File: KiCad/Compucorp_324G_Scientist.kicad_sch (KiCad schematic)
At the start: 0 parts

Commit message: Updates to schematic
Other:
- added sheet Processor Board (Compucorp_324G_Processor_Board.kicad_sch)
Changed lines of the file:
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@@
+	)
+	(sheet
+		(at 237.49 99.06)
+		(size 38.1 22.86)
+		(exclude_from_sim no)
+		(in_bom yes)
+		(on_board yes)
+		(dnp no)
+		(fields_autoplaced yes)
+		(stroke
+			(width 0.1524)
+			(type solid)
+		)
+		(fill
+			(color 0 0 0 0.0000)
+		)
+		(property "Sheetname" "Processor Board"
+			(at 237.49 98.3484 0)
+			(effects
+				(font
+					(size 1.27 1.27)
+				)
+				(justify left bottom)
+			)
+		)
+		(property "Sheetfile" "Compucorp_324G_Processor_Board.kicad_sch"
+			(at 237.49 122.5046 0)
+			(effects
+				(font
+					(size 1.27 1.27)
+				)
+				(justify left top)
+			)
+		)
+		(instances
+			(project "Compucorp_324G_Scientist"
+				(path "/2d77b643-896b-4ca4-ac76-7c6cc0d5263f"
+					(page "4")
+				)
+			)
+		)
 	)
 	(sheet

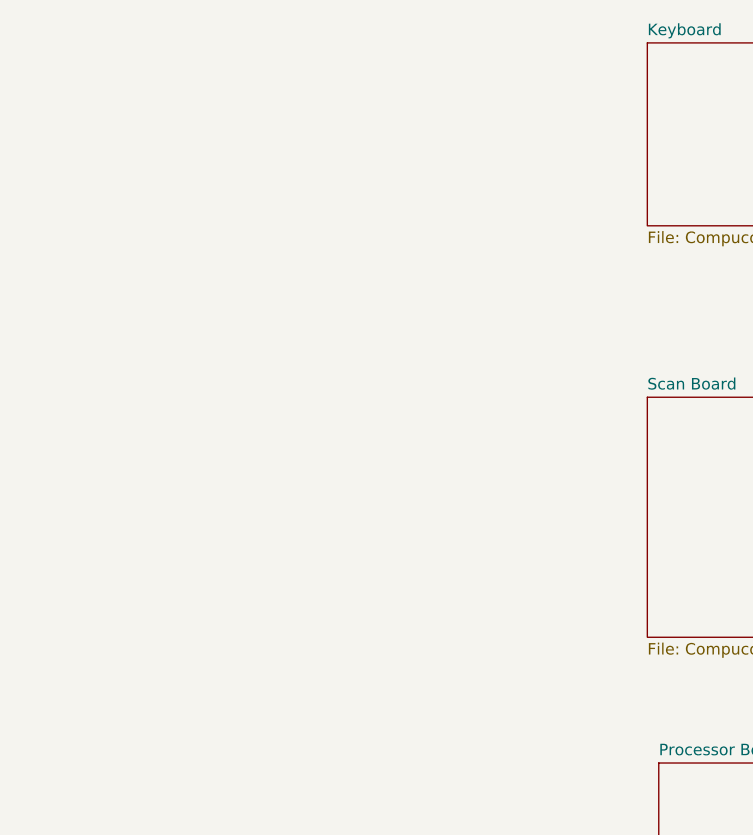
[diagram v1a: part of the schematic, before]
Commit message: Started on other board schematics
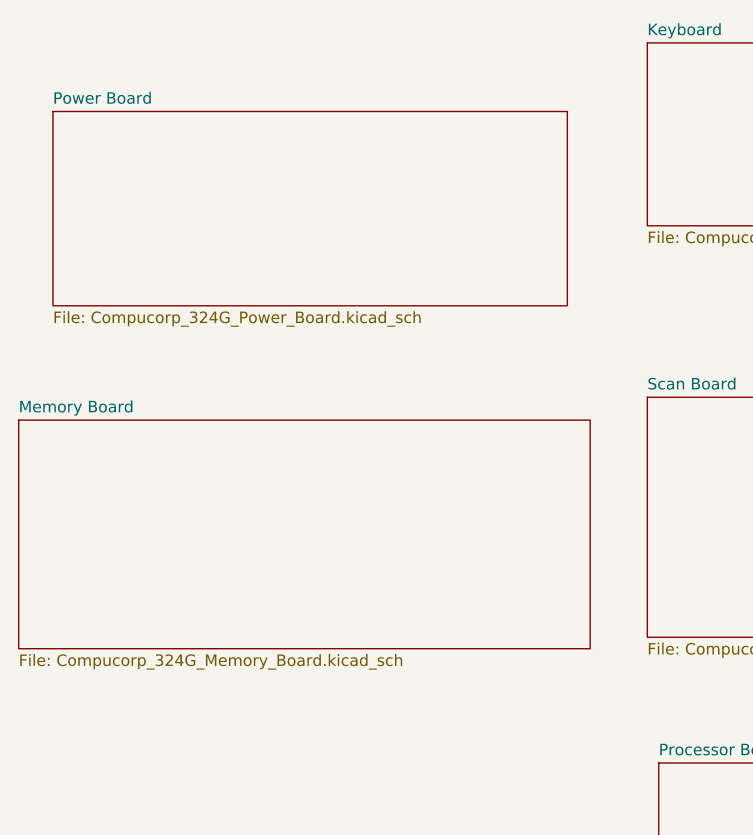
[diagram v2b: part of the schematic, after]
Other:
- added sheet Memory Board (Compucorp_324G_Memory_Board.kicad_sch)
- added sheet Power Board (Compucorp_324G_Power_Board.kicad_sch)
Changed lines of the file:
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@@
+	)
+	(sheet
+		(at 170.18 26.67)
+		(size 57.15 21.59)
+		(exclude_from_sim no)
+		(in_bom yes)
+		(on_board yes)
+		(dnp no)
+		(fields_autoplaced yes)
+		(stroke
+			(width 0.1524)
+			(type solid)
+		)
+		(fill
+			(color 0 0 0 0.0000)
+		)
+		(property "Sheetname" "Power Board"
+			(at 170.18 25.9584 0)
+			(effects
+				(font
+					(size 1.27 1.27)
+				)
+				(justify left bottom)
+			)
+		)
+		(property "Sheetfile" "Compucorp_324G_Power_Board.kicad_sch"
+			(at 170.18 48.8446 0)
+			(effects
+				(font
+					(size 1.27 1.27)
+				)
+				(justify left top)
+			)
+		)
+		(instances
+			(project "Compucorp_324G_Scientist"
+				(path "/2d77b643-896b-4ca4-ac76-7c6cc0d5263f"
+					(page "5")
+				)
+			)
+		)
 	)
 	(sheet
@@
 				)
 			)
+		)
+	)
+	(sheet
+		(at 166.37 60.96)
+		(size 63.5 25.4)
+		(exclude_from_sim no)
+		(in_bom yes)
+		(on_board yes)
+		(dnp no)
+		(fields_autoplaced yes)
+		(stroke
+			(width 0.1524)
+			(type solid)
+		)
+		(fill
+			(color 0 0 0 0.0000)
+		)
+		(property "Sheetname" "Memory Board"
+			(at 166.37 60.2484 0)
+			(effects
+				(font
+					(size 1.27 1.27)
+				)
+				(justify left bottom)
+			)
+		)
+		(property "Sheetfile" "Compucorp_324G_Memory_Board.kicad_sch"
+			(at 166.37 86.9446 0)
+			(effects
+				(font
+					(size 1.27 1.27)
+				)
+				(justify left top)
+			)
+		)
+		(instances
+			(project "Compucorp_324G_Scientist"
+				(path "/2d77b643-896b-4ca4-ac76-7c6cc0d5263f"
+					(page "6")
+				)
+			)

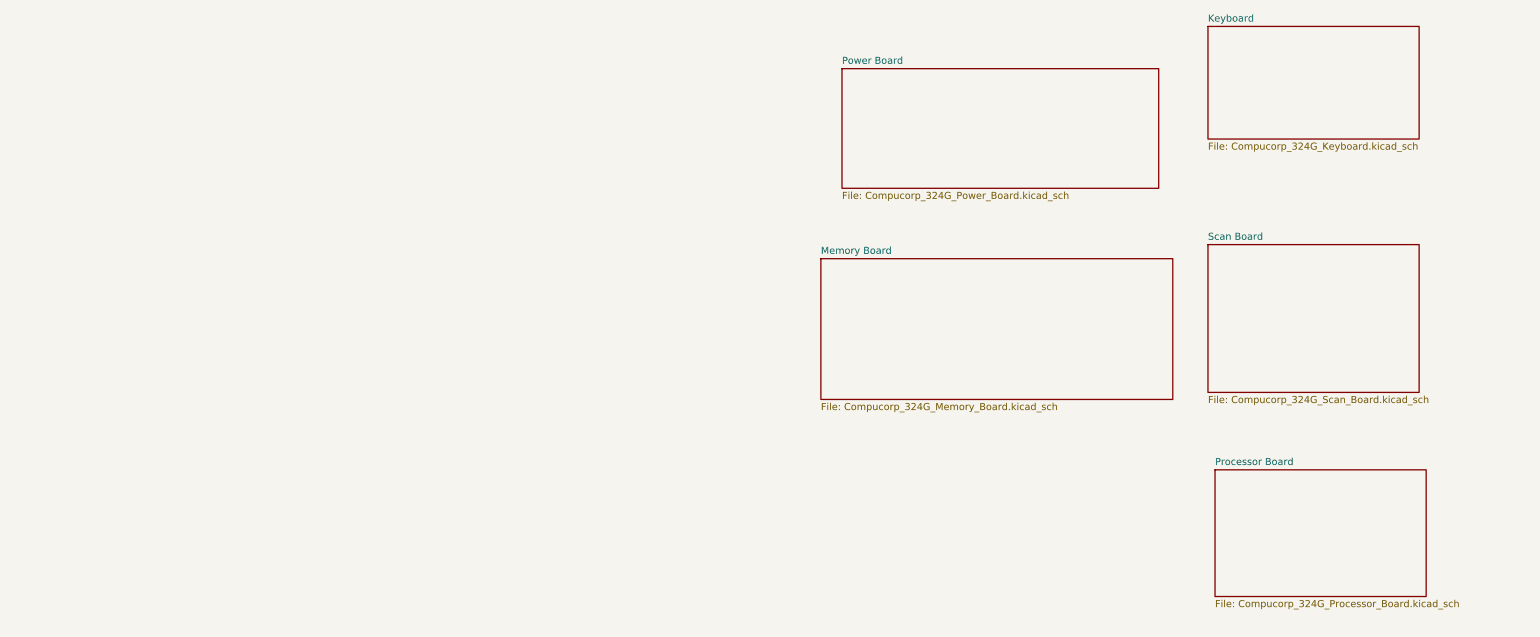
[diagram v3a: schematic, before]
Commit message: Schematic updates
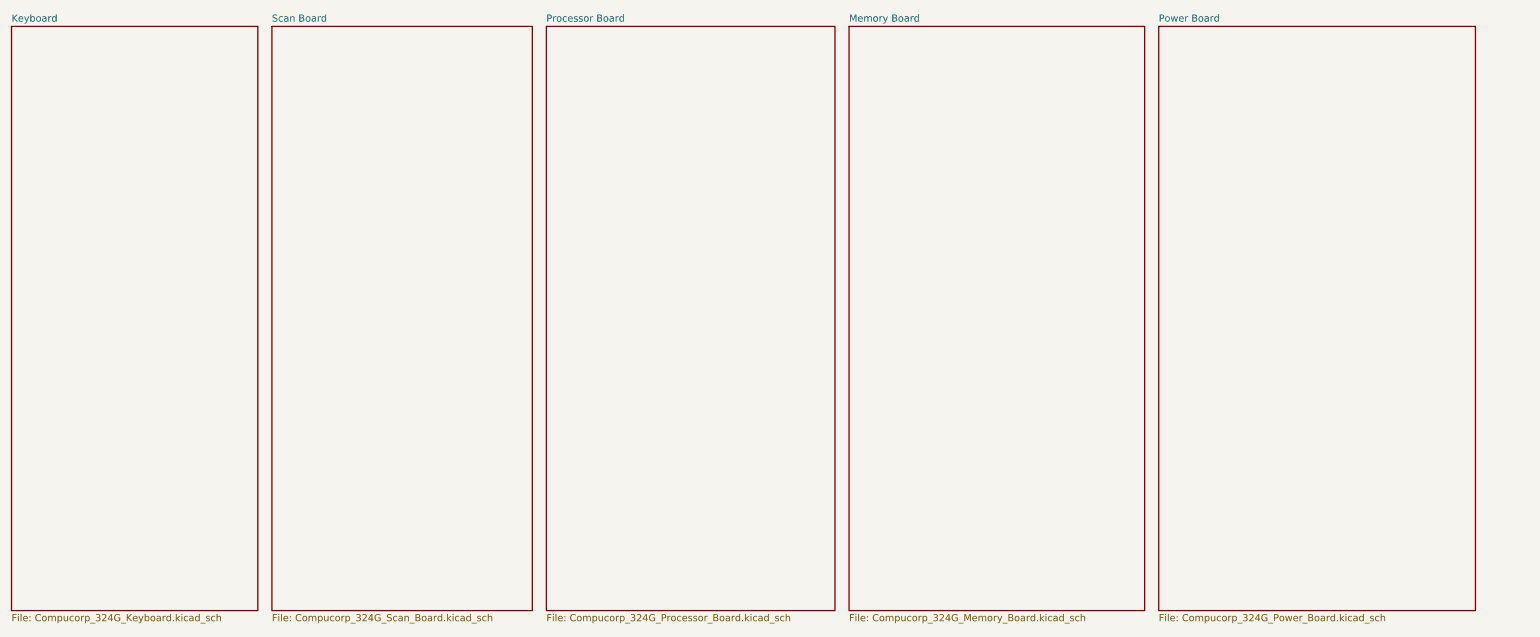
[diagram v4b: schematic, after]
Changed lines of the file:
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@@
 	)
 	(sheet
-		(at 237.49 99.06)
-		(size 38.1 22.86)
+		(at 116.84 19.05)
+		(size 52.07 105.41)
 		(exclude_from_sim no)
 		(in_bom yes)
@@
 		)
 		(property "Sheetname" "Processor Board"
-			(at 237.49 98.3484 0)
+			(at 116.84 18.3384 0)
 			(effects
 				(font
@@
 		)
 		(property "Sheetfile" "Compucorp_324G_Processor_Board.kicad_sch"
-			(at 237.49 122.5046 0)
+			(at 116.84 125.0446 0)
 			(effects
 				(font
@@
 	)
 	(sheet
-		(at 170.18 26.67)
-		(size 57.15 21.59)
+		(at 227.33 19.05)
+		(size 57.15 105.41)
 		(exclude_from_sim no)
 		(in_bom yes)
@@
 		)
 		(property "Sheetname" "Power Board"
-			(at 170.18 25.9584 0)
+			(at 227.33 18.3384 0)
 			(effects
 				(font
@@
 		)
 		(property "Sheetfile" "Compucorp_324G_Power_Board.kicad_sch"
-			(at 170.18 48.8446 0)
+			(at 227.33 125.0446 0)
+			(effects
+				(font
+					(size 1.27 1.27)
+				)
+				(justify left top)
+			)
+		)
+		(instances
+			(project "Compucorp_324G_Scientist"
+				(path "/2d77b643-896b-4ca4-ac76-7c6cc0d5263f"
+					(page "6")
+				)
+			)
+		)
+	)
+	(sheet
+		(at 20.32 19.05)
+		(size 44.45 105.41)
+		(exclude_from_sim no)
+		(in_bom yes)
+		(on_board yes)
+		(dnp no)
+		(fields_autoplaced yes)
+		(stroke
+			(width 0.1524)
+			(type solid)
+		)
+		(fill
+			(color 0 0 0 0.0000)
+		)
+		(property "Sheetname" "Keyboard"
+			(at 20.32 18.3384 0)
+			(effects
+				(font
+					(size 1.27 1.27)
+				)
+				(justify left bottom)
+			)
+		)
+		(property "Sheetfile" "Compucorp_324G_Keyboard.kicad_sch"
+			(at 20.32 125.0446 0)
+			(effects
+				(font
+					(size 1.27 1.27)
+				)
+				(justify left top)
+			)
+		)
+		(instances
+			(project "Compucorp_324G_Scientist"
+				(path "/2d77b643-896b-4ca4-ac76-7c6cc0d5263f"
+					(page "2")
+				)
+			)
+		)
+	)
+	(sheet
+		(at 67.31 19.05)
+		(size 46.99 105.41)
+		(exclude_from_sim no)
+		(in_bom yes)
+		(on_board yes)
+		(dnp no)
+		(fields_autoplaced yes)
+		(stroke
+			(width 0.1524)
+			(type solid)
+		)
+		(fill
+			(color 0 0 0 0.0000)
+		)
+		(property "Sheetname" "Scan Board"
+			(at 67.31 18.3384 0)
+			(effects
+				(font
+					(size 1.27 1.27)
+				)
+				(justify left bottom)
+			)
+		)
+		(property "Sheetfile" "Compucorp_324G_Scan_Board.kicad_sch"
+			(at 67.31 125.0446 0)
+			(effects
+				(font
+					(size 1.27 1.27)
+				)
+				(justify left top)
+			)
+		)
+		(instances
+			(project "Compucorp_324G_Scientist"
+				(path "/2d77b643-896b-4ca4-ac76-7c6cc0d5263f"
+					(page "3")
+				)
+			)
+		)
+	)
+	(sheet
+		(at 171.45 19.05)
+		(size 53.34 105.41)
+		(exclude_from_sim no)
+		(in_bom yes)
+		(on_board yes)
+		(dnp no)
+		(fields_autoplaced yes)
+		(stroke
+			(width 0.1524)
+			(type solid)
+		)
+		(fill
+			(color 0 0 0 0.0000)
+		)
+		(property "Sheetname" "Memory Board"
+			(at 171.45 18.3384 0)
+			(effects
+				(font
+					(size 1.27 1.27)
+				)
+				(justify left bottom)
+			)
+		)
+		(property "Sheetfile" "Compucorp_324G_Memory_Board.kicad_sch"
+			(at 171.45 125.0446 0)
 			(effects
 				(font
@@
 				)
 			)
-		)
-	)
-	(sheet
-		(at 236.22 19.05)
-		(size 38.1 20.32)
-		(exclude_from_sim no)
-		(in_bom yes)
-		(on_board yes)
-		(dnp no)
-		(fields_autoplaced yes)
-		(stroke
-			(width 0.1524)
-			(type solid)
-		)
-		(fill
-			(color 0 0 0 0.0000)
-		)
-		(property "Sheetname" "Keyboard"
-			(at 236.22 18.3384 0)
-			(effects
-				(font
-					(size 1.27 1.27)
-				)
-				(justify left bottom)
-			)
-		)
-		(property "Sheetfile" "Compucorp_324G_Keyboard.kicad_sch"
-			(at 236.22 39.9546 0)
-			(effects
-				(font
-					(size 1.27 1.27)
-				)
-				(justify left top)
-			)
-		)
-		(instances
-			(project "Compucorp_324G_Scientist"
-				(path "/2d77b643-896b-4ca4-ac76-7c6cc0d5263f"
-					(page "2")
-				)
-			)
-		)
-	)
-	(sheet
-		(at 236.22 58.42)
-		(size 38.1 26.67)
-		(exclude_from_sim no)
-		(in_bom yes)
-		(on_board yes)
-		(dnp no)
-		(fields_autoplaced yes)
-		(stroke
-			(width 0.1524)
-			(type solid)
-		)
-		(fill
-			(color 0 0 0 0.0000)
-		)
-		(property "Sheetname" "Scan Board"
-			(at 236.22 57.7084 0)
-			(effects
-				(font
-					(size 1.27 1.27)
-				)
-				(justify left bottom)
-			)
-		)
-		(property "Sheetfile" "Compucorp_324G_Scan_Board.kicad_sch"
-			(at 236.22 85.6746 0)
-			(effects
-				(font
-					(size 1.27 1.27)
-				)
-				(justify left top)
-			)
-		)
-		(instances
-			(project "Compucorp_324G_Scientist"
-				(path "/2d77b643-896b-4ca4-ac76-7c6cc0d5263f"
-					(page "3")
-				)
-			)
-		)
-	)
-	(sheet
-		(at 166.37 60.96)
-		(size 63.5 25.4)
-		(exclude_from_sim no)
-		(in_bom yes)
-		(on_board yes)
-		(dnp no)
-		(fields_autoplaced yes)
-		(stroke
-			(width 0.1524)
-			(type solid)
-		)
-		(fill
-			(color 0 0 0 0.0000)
-		)
-		(property "Sheetname" "Memory Board"
-			(at 166.37 60.2484 0)
-			(effects
-				(font
-					(size 1.27 1.27)
-				)
-				(justify left bottom)
-			)
-		)
-		(property "Sheetfile" "Compucorp_324G_Memory_Board.kicad_sch"
-			(at 166.37 86.9446 0)
-			(effects
-				(font
-					(size 1.27 1.27)
-				)
-				(justify left top)
-			)
-		)
-		(instances
-			(project "Compucorp_324G_Scientist"
-				(path "/2d77b643-896b-4ca4-ac76-7c6cc0d5263f"
-					(page "6")
-				)
-			)
